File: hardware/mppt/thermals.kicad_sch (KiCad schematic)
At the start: 27 parts, among them J401 Conn_01x04, J402 Conn_01x03, U401 MCP9700Ax-ELT, U402 MCP9700Ax-ELT

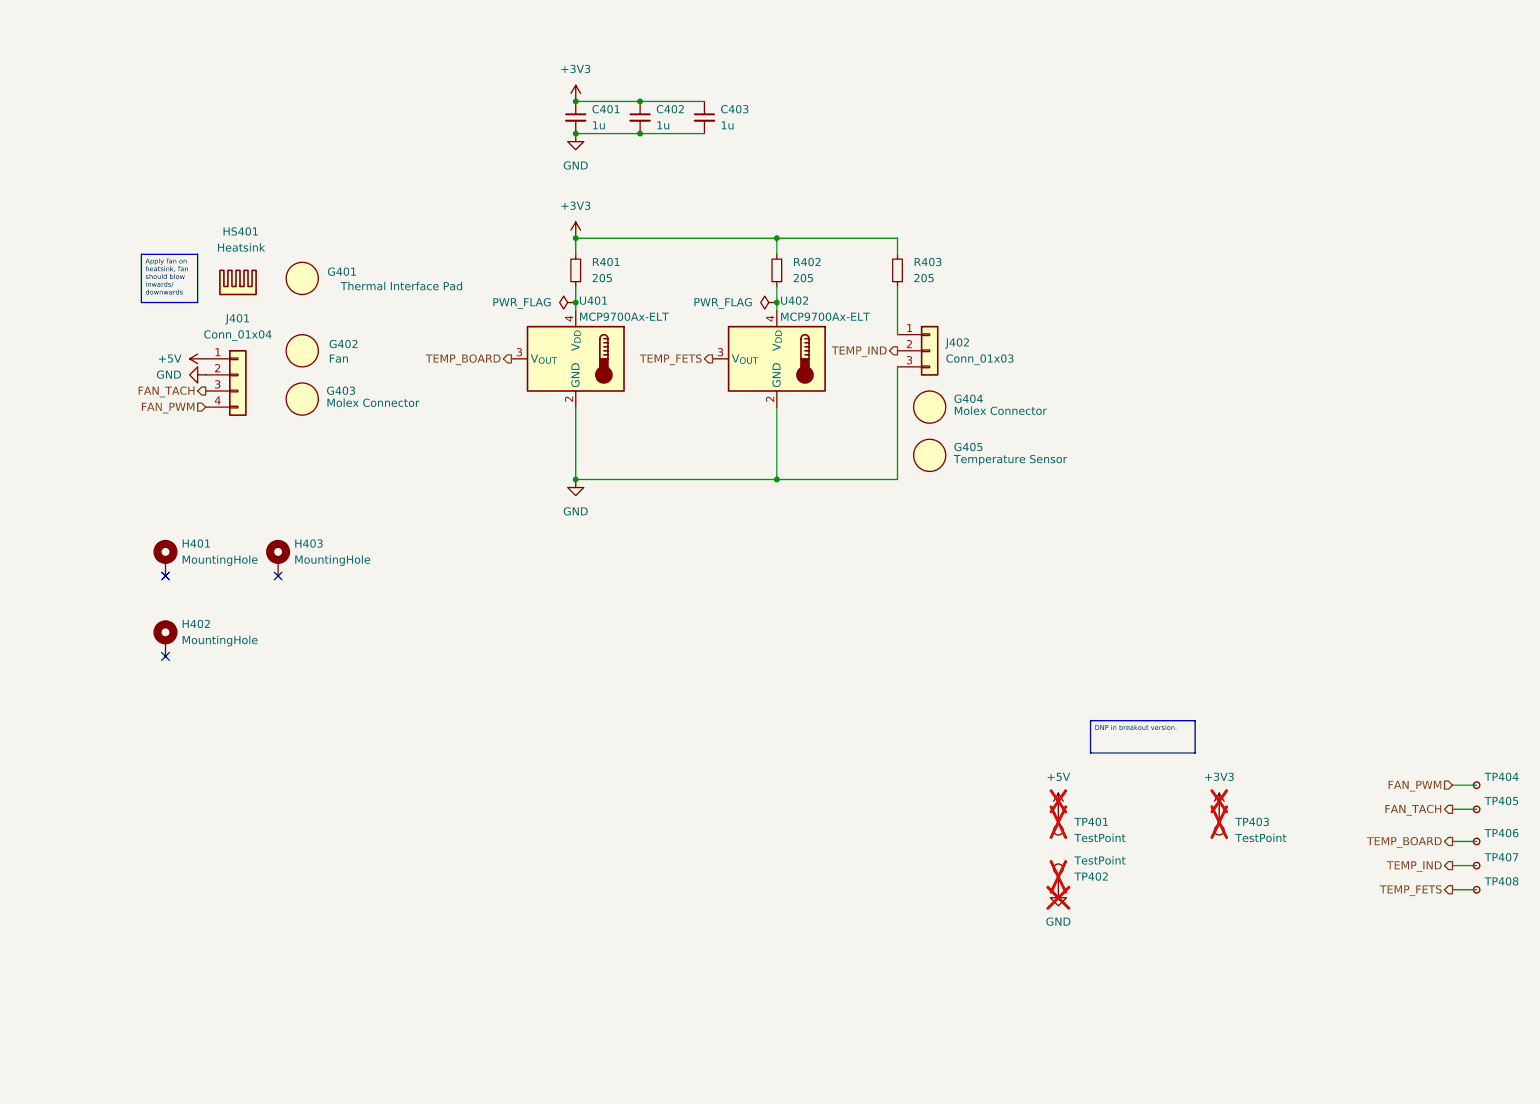
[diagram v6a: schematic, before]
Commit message: converter schematic and layout.
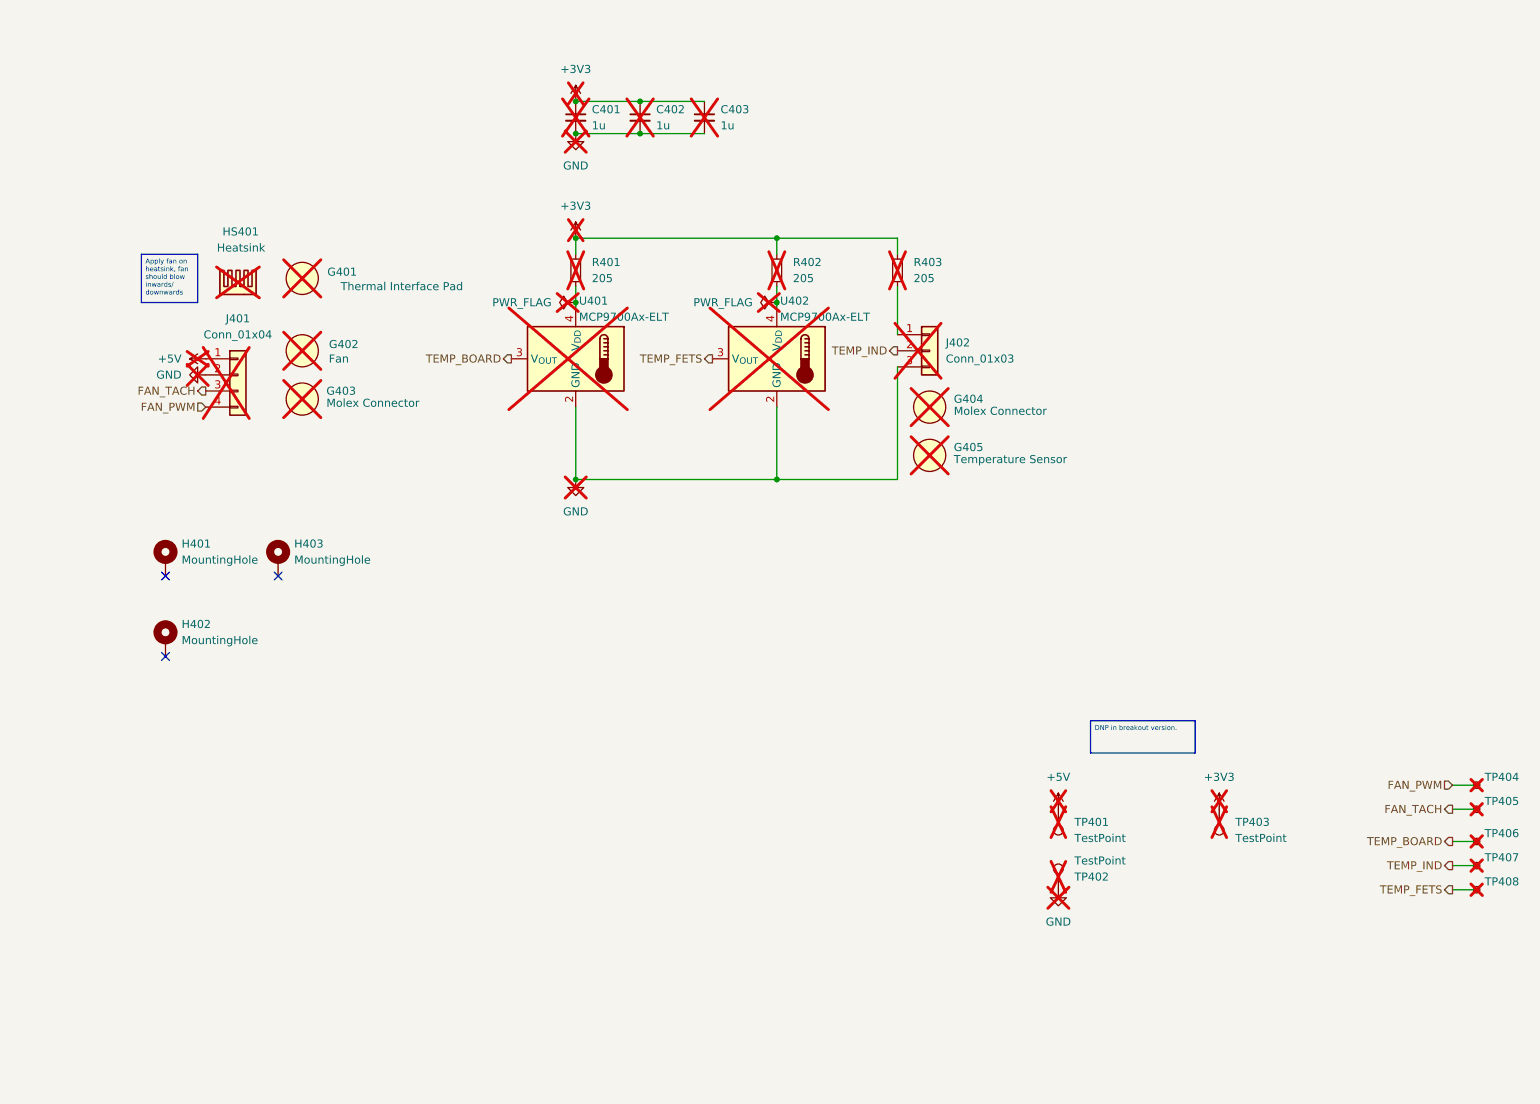
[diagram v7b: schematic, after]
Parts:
- C401, C402, C403, G401, G402, G403, G404, G405, HS401, J401, J402, R401, R402, R403, TP404, TP405, TP406, TP407, TP408, U401, U402: now not fitted; now left out of the parts list
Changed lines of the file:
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@@
 		(unit 1)
 		(exclude_from_sim no)
-		(in_bom yes)
-		(on_board yes)
-		(dnp no)
+		(in_bom no)
+		(on_board no)
+		(dnp yes)
 		(fields_autoplaced yes)
 		(property "Reference" "#PWR0401"
@@
 		(unit 1)
 		(exclude_from_sim no)
-		(in_bom yes)
-		(on_board yes)
-		(dnp no)
+		(in_bom no)
+		(on_board no)
+		(dnp yes)
 		(fields_autoplaced yes)
 		(property "Reference" "#FLG0402"
@@
 		(unit 1)
 		(exclude_from_sim no)
-		(in_bom yes)
-		(on_board yes)
-		(dnp no)
+		(in_bom no)
+		(on_board no)
+		(dnp yes)
 		(fields_autoplaced yes)
 		(property "Reference" "J401"
@@
 		(unit 1)
 		(exclude_from_sim no)
-		(in_bom yes)
-		(on_board no)
-		(dnp no)
+		(in_bom no)
+		(on_board no)
+		(dnp yes)
 		(property "Reference" "G404"
 			(at 157.48 83.82 0)
@@
 		(unit 1)
 		(exclude_from_sim no)
-		(in_bom yes)
-		(on_board no)
-		(dnp no)
+		(in_bom no)
+		(on_board no)
+		(dnp yes)
 		(property "Reference" "G402"
 			(at 63.5 75.184 0)
@@
 		(unit 1)
 		(exclude_from_sim no)
-		(in_bom yes)
-		(on_board yes)
-		(dnp no)
+		(in_bom no)
+		(on_board no)
+		(dnp yes)
 		(fields_autoplaced yes)
 		(property "Reference" "TP405"
@@
 		(unit 1)
 		(exclude_from_sim no)
-		(in_bom yes)
-		(on_board yes)
-		(dnp no)
+		(in_bom no)
+		(on_board no)
+		(dnp yes)
 		(fields_autoplaced yes)
 		(property "Reference" "C402"
@@
 		(unit 1)
 		(exclude_from_sim no)
-		(in_bom yes)
-		(on_board yes)
-		(dnp no)
+		(in_bom no)
+		(on_board no)
+		(dnp yes)
 		(fields_autoplaced yes)
 		(property "Reference" "#PWR0404"
@@
 		(unit 1)
 		(exclude_from_sim no)
-		(in_bom yes)
-		(on_board yes)
-		(dnp no)
+		(in_bom no)
+		(on_board no)
+		(dnp yes)
 		(fields_autoplaced yes)
 		(property "Reference" "#PWR0406"
@@
 		(unit 1)
 		(exclude_from_sim no)
-		(in_bom yes)
-		(on_board yes)
-		(dnp no)
+		(in_bom no)
+		(on_board no)
+		(dnp yes)
 		(fields_autoplaced yes)
 		(property "Reference" "#PWR0403"
@@
 		(unit 1)
 		(exclude_from_sim no)
-		(in_bom yes)
-		(on_board no)
-		(dnp no)
+		(in_bom no)
+		(on_board no)
+		(dnp yes)
 		(property "Reference" "HS401"
 			(at 47.752 57.404 0)
@@
 		(unit 1)
 		(exclude_from_sim no)
-		(in_bom yes)
-		(on_board yes)
-		(dnp no)
+		(in_bom no)
+		(on_board no)
+		(dnp yes)
 		(fields_autoplaced yes)
 		(property "Reference" "C401"
@@
 		(unit 1)
 		(exclude_from_sim no)
-		(in_bom yes)
-		(on_board no)
-		(dnp no)
+		(in_bom no)
+		(on_board no)
+		(dnp yes)
 		(property "Reference" "G405"
 			(at 157.48 91.44 0)
@@
 		(unit 1)
 		(exclude_from_sim no)
-		(in_bom yes)
-		(on_board yes)
-		(dnp no)
+		(in_bom no)
+		(on_board no)
+		(dnp yes)
 		(fields_autoplaced yes)
 		(property "Reference" "TP407"
@@
 		(unit 1)
 		(exclude_from_sim no)
-		(in_bom yes)
-		(on_board yes)
-		(dnp no)
+		(in_bom no)
+		(on_board no)
+		(dnp yes)
 		(property "Reference" "U402"
 			(at 130.048 68.326 0)
@@
 		(unit 1)
 		(exclude_from_sim no)
-		(in_bom yes)
-		(on_board yes)
-		(dnp no)
+		(in_bom no)
+		(on_board no)
+		(dnp yes)
 		(fields_autoplaced yes)
 		(property "Reference" "#FLG0401"
@@
 		(unit 1)
 		(exclude_from_sim no)
-		(in_bom yes)
-		(on_board no)
-		(dnp no)
+		(in_bom no)
+		(on_board no)
+		(dnp yes)
 		(property "Reference" "G401"
 			(at 63.246 63.754 0)
@@
 		(unit 1)
 		(exclude_from_sim no)
-		(in_bom yes)
-		(on_board no)
-		(dnp no)
+		(in_bom no)
+		(on_board no)
+		(dnp yes)
 		(property "Reference" "G403"
 			(at 58.42 82.55 0)
@@
 		(unit 1)
 		(exclude_from_sim no)
-		(in_bom yes)
-		(on_board yes)
-		(dnp no)
+		(in_bom no)
+		(on_board no)
+		(dnp yes)
 		(fields_autoplaced yes)
 		(property "Reference" "TP404"
@@
 		(unit 1)
 		(exclude_from_sim no)
-		(in_bom yes)
-		(on_board yes)
-		(dnp no)
+		(in_bom no)
+		(on_board no)
+		(dnp yes)
 		(fields_autoplaced yes)
 		(property "Reference" "R401"
@@
 		(unit 1)
 		(exclude_from_sim no)
-		(in_bom yes)
-		(on_board yes)
-		(dnp no)
+		(in_bom no)
+		(on_board no)
+		(dnp yes)
 		(fields_autoplaced yes)
 		(property "Reference" "#PWR0402"
@@
 		(unit 1)
 		(exclude_from_sim no)
-		(in_bom yes)
-		(on_board yes)
-		(dnp no)
+		(in_bom no)
+		(on_board no)
+		(dnp yes)
 		(fields_autoplaced yes)
 		(property "Reference" "TP408"
@@
 		(unit 1)
 		(exclude_from_sim no)
-		(in_bom yes)
-		(on_board yes)
-		(dnp no)
+		(in_bom no)
+		(on_board no)
+		(dnp yes)
 		(property "Reference" "U401"
 			(at 98.298 68.326 0)
@@
 		(unit 1)
 		(exclude_from_sim no)
-		(in_bom yes)
-		(on_board yes)
-		(dnp no)
+		(in_bom no)
+		(on_board no)
+		(dnp yes)
 		(fields_autoplaced yes)
 		(property "Reference" "J402"
@@
 		(unit 1)
 		(exclude_from_sim no)
-		(in_bom yes)
-		(on_board yes)
-		(dnp no)
+		(in_bom no)
+		(on_board no)
+		(dnp yes)
 		(fields_autoplaced yes)
 		(property "Reference" "R402"
@@
 		(unit 1)
 		(exclude_from_sim no)
-		(in_bom yes)
-		(on_board yes)
-		(dnp no)
+		(in_bom no)
+		(on_board no)
+		(dnp yes)
 		(fields_autoplaced yes)
 		(property "Reference" "#PWR0405"
@@
 		(unit 1)
 		(exclude_from_sim no)
-		(in_bom yes)
-		(on_board yes)
-		(dnp no)
+		(in_bom no)
+		(on_board no)
+		(dnp yes)
 		(fields_autoplaced yes)
 		(property "Reference" "TP406"
@@
 		(unit 1)
 		(exclude_from_sim no)
-		(in_bom yes)
-		(on_board yes)
-		(dnp no)
+		(in_bom no)
+		(on_board no)
+		(dnp yes)
 		(fields_autoplaced yes)
 		(property "Reference" "R403"
@@
 		(unit 1)
 		(exclude_from_sim no)
-		(in_bom yes)
-		(on_board yes)
-		(dnp no)
+		(in_bom no)
+		(on_board no)
+		(dnp yes)
 		(fields_autoplaced yes)
 		(property "Reference" "C403"
